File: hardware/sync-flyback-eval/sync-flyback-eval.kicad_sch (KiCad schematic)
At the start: 89 parts, among them J1 RJ45_LED_Shielded, Q1 SiR422DP, Q2 Si7898DP, Q3 MMDT3906, T1 PoE_Transformer, T2 Pulse_Transformer, U1 TPS23754PWPR, U2 TCMT1107

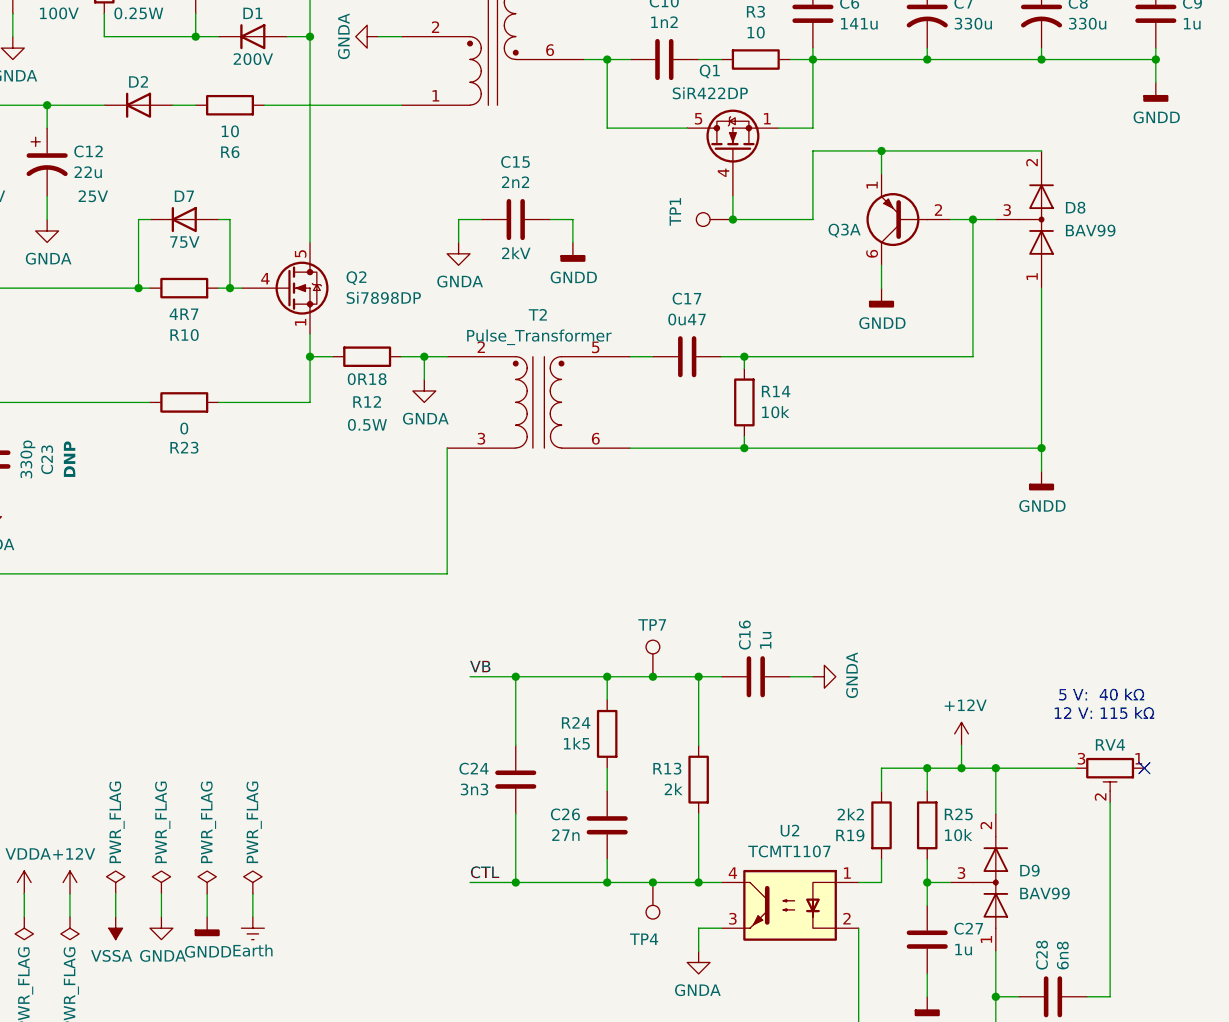
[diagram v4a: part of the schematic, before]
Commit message: flyback: dnp the two diode arrays
Let's see what happens without them (I don't have them on-hand).
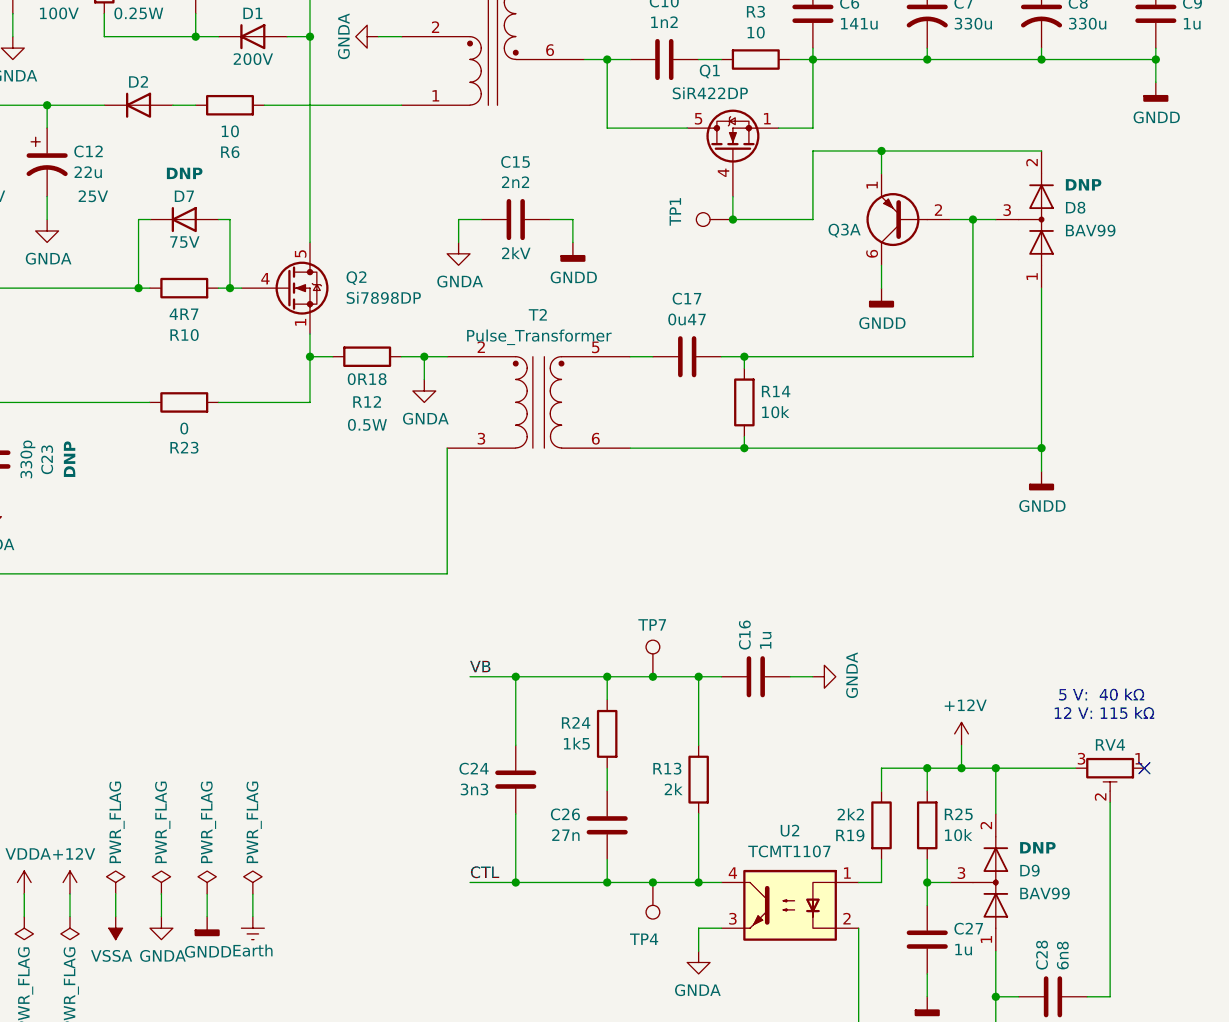
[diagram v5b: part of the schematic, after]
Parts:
- D7, D8, D9: Placement (none) -> DNP
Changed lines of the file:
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@@
     )
     (property "Voltage" "75V" (id 4) (at 153.67 59.69 0))
+    (property "Placement" "DNP" (id 5) (at 153.67 52.07 0)
+      (effects (font (size 1.27 1.27) bold))
+    )
     (pin "1")
     (pin "2")
@@
   )
   (symbol (lib_id "Diode:BAV99") (at 248.92 57.15 270) (mirror x) (unit 1)
-    (in_bom yes) (on_board yes) (fields_autoplaced)
+    (in_bom yes) (on_board yes)
     (property "Reference" "D8" (id 0) (at 251.46 55.8799 90)
       (effects (font (size 1.27 1.27)) (justify left))
@@
       (effects (font (size 1.27 1.27)) hide)
     )
+    (property "Placement" "DNP" (id 4) (at 251.46 53.34 90)
+      (effects (font (size 1.27 1.27) bold) (justify left))
+    )
     (pin "1")
     (pin "2")
@@
   )
   (symbol (lib_id "Diode:BAV99") (at 243.84 130.81 270) (mirror x) (unit 1)
-    (in_bom yes) (on_board yes) (fields_autoplaced)
+    (in_bom yes) (on_board yes)
     (property "Reference" "D9" (id 0) (at 246.38 129.5399 90)
       (effects (font (size 1.27 1.27)) (justify left))
@@
       (effects (font (size 1.27 1.27)) hide)
     )
-    (pin "1")
+    (property "Placement" "DNP" (id 4) (at 246.38 127 90)
+      (effects (font (size 1.27 1.27) bold) (justify left))
+    )
+    (pin "1")

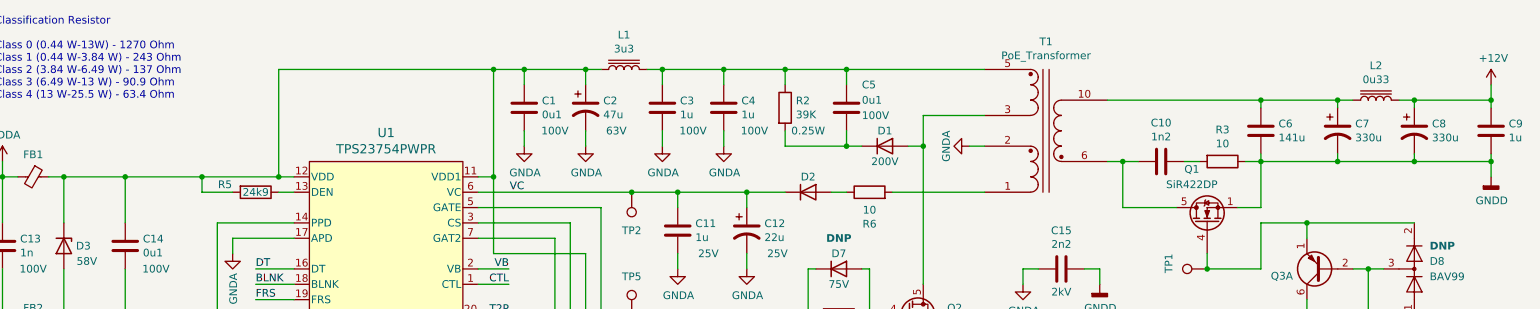
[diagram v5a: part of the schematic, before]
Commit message: flyback: add current-sense resistors to input and output
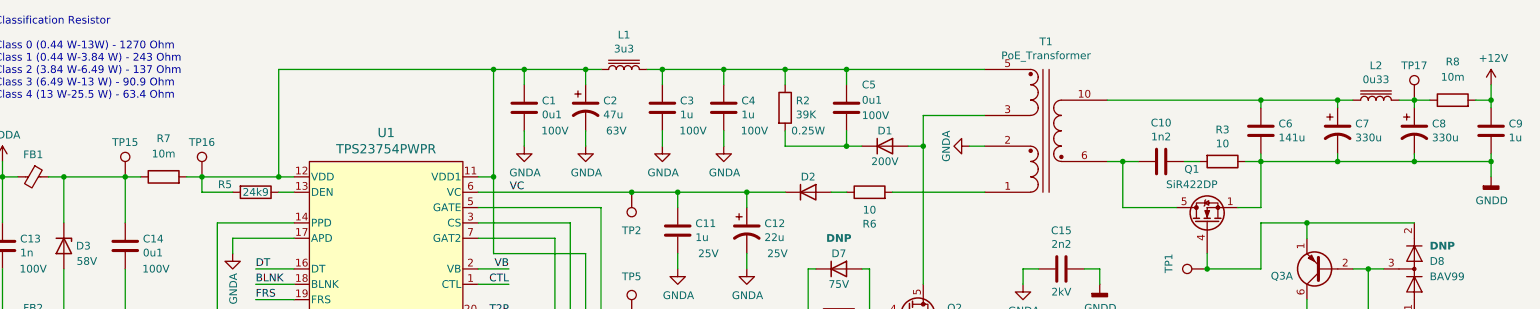
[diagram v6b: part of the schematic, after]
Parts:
- added R7, R8: 10m, Resistor_SMD:R_0402_1005Metric, symbol Device:R
- added TP15, TP16, TP17: VB, TestPoint:TestPoint_Pad_1.5x1.5mm, symbol Connector:TestPoint
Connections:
- net +12V: now also R8.2; no longer C8.1, L2.2
- net at C1.1, C2.1, L1.1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: now also R7.2, TP16.1; no longer C14.1, D3.1 (K), FB1.1
- new net: C14.1, D3.1 (K), FB1.1, R7.1, TP15.1
- new net: C8.1, L2.2, R8.1, TP17.1
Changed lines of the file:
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@@
   (junction (at 243.84 143.51) (diameter 0) (color 0 0 0 0)
   )
+  (junction (at 35.56 41.91) (diameter 0) (color 0 0 0 0)
+  )
   (junction (at 180.34 72.39) (diameter 0) (color 0 0 0 0)
   )
-  (junction (at 35.56 41.91) (diameter 0) (color 0 0 0 0)
+  (junction (at 48.26 41.91) (diameter 0) (color 0 0 0 0)
   )
   (junction (at 243.84 118.11) (diameter 0) (color 0 0 0 0)
@@
   (junction (at 96.52 24.13) (diameter 0) (color 0 0 0 0)
   )
-  (junction (at 48.26 41.91) (diameter 0) (color 0 0 0 0)
-  )
   (junction (at 144.78 24.13) (diameter 0) (color 0 0 0 0)
   )
@@
     (stroke (width 0) (type default) (color 0 0 0 0))
   )
+  (wire (pts (xy 259.08 29.21) (xy 261.62 29.21))
+    (stroke (width 0) (type default) (color 0 0 0 0))
+  )
   (wire (pts (xy 228.6 130.81) (xy 231.14 130.81))
     (stroke (width 0) (type default) (color 0 0 0 0))
@@
     (stroke (width 0) (type default) (color 0 0 0 0))
   )
+  (wire (pts (xy 35.56 41.91) (xy 38.1 41.91))
+    (stroke (width 0) (type default) (color 0 0 0 0))
+  )
   (wire (pts (xy 55.88 119.38) (xy 78.74 119.38))
     (stroke (width 0) (type default) (color 0 0 0 0))
@@
     (stroke (width 0) (type default) (color 0 0 0 0))
   )
-  (wire (pts (xy 48.26 41.91) (xy 35.56 41.91))
-    (stroke (width 0) (type default) (color 0 0 0 0))
-  )
   (wire (pts (xy 63.5 74.93) (xy 60.96 74.93))
     (stroke (width 0) (type default) (color 0 0 0 0))
@@
     (stroke (width 0) (type default) (color 0 0 0 0))
   )
-  (wire (pts (xy 248.92 29.21) (xy 261.62 29.21))
+  (wire (pts (xy 248.92 29.21) (xy 251.46 29.21))
     (stroke (width 0) (type default) (color 0 0 0 0))
   )
@@
     (stroke (width 0) (type default) (color 0 0 0 0))
   )
+  (wire (pts (xy 45.72 41.91) (xy 48.26 41.91))
+    (stroke (width 0) (type default) (color 0 0 0 0))
+  )
   (wire (pts (xy 240.03 115.57) (xy 240.03 118.11))
     (stroke (width 0) (type default) (color 0 0 0 0))
@@
     (pin "1")
   )
+  (symbol (lib_id "Device:R") (at 41.91 41.91 90) (unit 1)
+    (in_bom yes) (on_board yes) (fields_autoplaced)
+    (property "Reference" "R7" (id 0) (at 41.91 35.56 90))
+    (property "Value" "10m" (id 1) (at 41.91 38.1 90))
+    (property "Footprint" "Resistor_SMD:R_0402_1005Metric" (id 2) (at 41.91 43.688 90)
+      (effects (font (size 1.27 1.27)) hide)
+    )
+    (property "Datasheet" "~" (id 3) (at 41.91 41.91 0)
+      (effects (font (size 1.27 1.27)) hide)
+    )
+    (pin "1")
+    (pin "2")
+  )
   (symbol (lib_id "Connector:TestPoint") (at 119.38 64.77 0) (unit 1)
     (in_bom yes) (on_board yes)
@@
     (pin "2")
   )
+  (symbol (lib_id "Device:R") (at 255.27 29.21 90) (unit 1)
+    (in_bom yes) (on_board yes) (fields_autoplaced)
+    (property "Reference" "R8" (id 0) (at 255.27 22.86 90))
+    (property "Value" "10m" (id 1) (at 255.27 25.4 90))
+    (property "Footprint" "Resistor_SMD:R_0402_1005Metric" (id 2) (at 255.27 30.988 90)
+      (effects (font (size 1.27 1.27)) hide)
+    )
+    (property "Datasheet" "~" (id 3) (at 255.27 29.21 0)
+      (effects (font (size 1.27 1.27)) hide)
+    )
+    (pin "1")
+    (pin "2")
+  )
   (symbol (lib_id "Connector:TestPoint") (at 205.74 107.95 0) (unit 1)
     (in_bom yes) (on_board yes)
@@
     (pin "1")
   )
+  (symbol (lib_id "Connector:TestPoint") (at 35.56 41.91 0) (unit 1)
+    (in_bom yes) (on_board yes)
+    (property "Reference" "TP15" (id 0) (at 35.56 36.195 0))
+    (property "Value" "VB" (id 1) (at 36.703 37.1348 90)
+      (effects (font (size 1.27 1.27)) (justify left) hide)
+    )
+    (property "Footprint" "TestPoint:TestPoint_Pad_1.5x1.5mm" (id 2) (at 40.64 41.91 0)
+      (effects (font (size 1.27 1.27)) hide)
+    )
+    (property "Datasheet" "~" (id 3) (at 40.64 41.91 0)
+      (effects (font (size 1.27 1.27)) hide)
+    )
+    (pin "1")
+  )
+  (symbol (lib_id "Connector:TestPoint") (at 248.92 29.21 0) (unit 1)
+    (in_bom yes) (on_board yes)
+    (property "Reference" "TP17" (id 0) (at 248.92 23.495 0))
+    (property "Value" "VB" (id 1) (at 250.063 24.4348 90)
+      (effects (font (size 1.27 1.27)) (justify left) hide)
+    )
+    (property "Footprint" "TestPoint:TestPoint_Pad_1.5x1.5mm" (id 2) (at 254 29.21 0)
+      (effects (font (size 1.27 1.27)) hide)
+    )
+    (property "Datasheet" "~" (id 3) (at 254 29.21 0)
+      (effects (font (size 1.27 1.27)) hide)
+    )
+    (pin "1")
+  )
   (symbol (lib_id "Diode:BAV99") (at 248.92 57.15 270) (mirror x) (unit 1)
     (in_bom yes) (on_board yes)
@@
     (pin "1")
   )
+  (symbol (lib_id "Connector:TestPoint") (at 48.26 41.91 0) (unit 1)
+    (in_bom yes) (on_board yes)
+    (property "Reference" "TP16" (id 0) (at 48.26 36.195 0))
+    (property "Value" "VB" (id 1) (at 49.403 37.1348 90)
+      (effects (font (size 1.27 1.27)) (justify left) hide)
+    )
+    (property "Footprint" "TestPoint:TestPoint_Pad_1.5x1.5mm" (id 2) (at 53.34 41.91 0)
+      (effects (font (size 1.27 1.27)) hide)
+    )
+    (property "Datasheet" "~" (id 3) (at 53.34 41.91 0)
+      (effects (font (size 1.27 1.27)) hide)
+    )
+    (pin "1")
+  )
   (sheet_instances
     (path "/" (page "1"))
@@
       (reference "R6") (unit 1) (value "10") (footprint "Resistor_SMD:R_0402_1005Metric")
     )
+    (path "/4ede36d6-f7e9-4a55-b79f-e40a3ba5a33e"
+      (reference "R7") (unit 1) (value "10m") (footprint "Resistor_SMD:R_0402_1005Metric")
+    )
+    (path "/57318aa0-17f0-4d60-9e15-14e51a15717a"
+      (reference "R8") (unit 1) (value "10m") (footprint "Resistor_SMD:R_0402_1005Metric")
+    )
     (path "/00000000-0000-0000-0000-00005c50e979"
       (reference "R10") (unit 1) (value "4R7") (footprint "Resistor_SMD:R_0402_1005Metric")
@@
       (reference "TP14") (unit 1) (value "EARTH") (footprint "TestPoint:TestPoint_Pad_1.5x1.5mm")
     )
+    (path "/bceeb1d1-5f1f-41b0-add1-5f28ebadcf33"
+      (reference "TP15") (unit 1) (value "VB") (footprint "TestPoint:TestPoint_Pad_1.5x1.5mm")
+    )
+    (path "/fe5b4dec-9e8b-406d-98e5-77476a406435"
+      (reference "TP16") (unit 1) (value "VB") (footprint "TestPoint:TestPoint_Pad_1.5x1.5mm")
+    )
+    (path "/cc499ba5-7e90-407f-8a08-b071d5a46ebc"
+      (reference "TP17") (unit 1) (value "VB") (footprint "TestPoint:TestPoint_Pad_1.5x1.5mm")
+    )
     (path "/00000000-0000-0000-0000-00005d6ac6f9"

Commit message: flyback: associate trimpot footprints
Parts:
- RV1, RV2, RV3, RV4: footprint (none) -> common:TRIM_3306F-1-204
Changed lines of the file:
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@@
       (effects (font (size 1.27 1.27)) hide)
     )
-    (property "Footprint" "" (id 2) (at 38.1 82.55 0)
+    (property "Footprint" "common:TRIM_3306F-1-204" (id 2) (at 38.1 82.55 0)
       (effects (font (size 1.27 1.27)) hide)
     )
@@
       (effects (font (size 1.27 1.27)) hide)
     )
-    (property "Footprint" "" (id 2) (at 45.72 88.9 0)
+    (property "Footprint" "common:TRIM_3306F-1-204" (id 2) (at 45.72 88.9 0)
       (effects (font (size 1.27 1.27)) hide)
     )
@@
       (effects (font (size 1.27 1.27)) hide)
     )
-    (property "Footprint" "" (id 2) (at 30.48 76.2 0)
+    (property "Footprint" "common:TRIM_3306F-1-204" (id 2) (at 30.48 76.2 0)
       (effects (font (size 1.27 1.27)) hide)
     )
@@
       (effects (font (size 1.27 1.27)) hide)
     )
-    (property "Footprint" "" (id 2) (at 256.54 118.11 0)
+    (property "Footprint" "common:TRIM_3306F-1-204" (id 2) (at 256.54 118.11 0)
       (effects (font (size 1.27 1.27)) hide)
     )
@@
     )
     (path "/86c43cfa-98d8-4f01-ad6e-e695dc4800d5"
-      (reference "RV1") (unit 1) (value "0-200k") (footprint "")
+      (reference "RV1") (unit 1) (value "0-200k") (footprint "common:TRIM_3306F-1-204")
     )
     (path "/7831dd4a-a5ea-4555-a6e3-4f0924962575"
-      (reference "RV2") (unit 1) (value "0-200k") (footprint "")
+      (reference "RV2") (unit 1) (value "0-200k") (footprint "common:TRIM_3306F-1-204")
     )
     (path "/7f9d8239-623e-4e6d-a91a-d1f6126a0e76"
-      (reference "RV3") (unit 1) (value "0-200k") (footprint "")
+      (reference "RV3") (unit 1) (value "0-200k") (footprint "common:TRIM_3306F-1-204")
     )
     (path "/981d4e4a-c5d7-441c-8be5-cfd05c87b9e8"
-      (reference "RV4") (unit 1) (value "0-200k") (footprint "")
+      (reference "RV4") (unit 1) (value "0-200k") (footprint "common:TRIM_3306F-1-204")
     )
     (path "/00000000-0000-0000-0000-00005dad1b8a"
